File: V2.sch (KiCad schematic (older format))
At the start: 97 parts, among them J1 Extr Cooler 2, J10 MS2, J11 MS3, J12 MS1, J13 MS2, J14 MS3, J15 Extr1 Temp, J16 Extr2 Temp, J17 MS1, J18 MS2, J19 MS3, J2 Extr Cooler 1, J20 Boot0, J21 Bed Temp, J22 Boot1, J23 MS1, J24 MS2, J25 MS3, J26 USB_A, J27 LCD, J28 MS1, J29 MS2, J3 Bed Heater, J30 MS3, J31 USB_A, J4 Extr1 Heater, J5 Extr2 Heater, J6 MS1, J7 MS2, J8 MS3, J9 MS1, M1 Motor E2, M2 Motor E1, M3 Motor Z2, M4 Motor Z1, M5 Motor Y, M6 Motor X, Q1 STN4NF20L, Q2 STN4NF20L, Q3 04N03LA, Q4 04N03LA, Q5 04N03LA, SW1 Bed level, SW10 Button DOWN, SW11 Button UP, SW2 Boundary X, SW3 Boundary Y, SW4 Boundary Z1, SW5 Boundary Z2, SW6 Boundary E1, SW7 Boundary E2, SW8 Button BACK, SW9 Button OK, U1 LM2596S-5, U2 R-783.3-1.0, U3 STM32F105VCT6, U4 CP2104, Y1 8MHz

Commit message: this is layout
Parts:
- removed J31: USB_A, symbol Connector:USB_A
- removed SW1: Bed level, symbol Switch:SW_Push_Open
- added J?: USB_B, symbol Connector:USB_B
- added J?: Bed level, symbol Connector:Conn_01x03_Male
- added LS?: Beeper, symbol device:Speaker
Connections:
- wire segments 497 -> 498
- no-connect marks 39 -> 38
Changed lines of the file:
@@
 Connection ~ 19300 7300
 $Comp
-L Switch:SW_Push_Open SW1
-U 1 1 5C488341
-P 8150 15550
-F 0 "SW1" V 8104 15627 50  0000 L CNN
-F 1 "Bed level" V 8195 15627 50  0000 L CNN
-F 2 "" H 8150 15750 50  0001 C CNN
-F 3 "" H 8150 15750 50  0001 C CNN
-	1    8150 15550
-	0    1    1    0
-$EndComp
-$Comp
 L Switch:SW_Push_Open SW2
 U 1 1 5C491094
@@
 L power:GNDD #PWR0130
 U 1 1 5C497D89
-P 8150 15750
-F 0 "#PWR0130" H 8150 15500 50  0001 C CNN
-F 1 "GNDD" H 8154 15595 50  0000 C CNN
-F 2 "" H 8150 15750 50  0001 C CNN
-F 3 "" H 8150 15750 50  0001 C CNN
-	1    8150 15750
-	1    0    0    -1
+P 8050 15550
+F 0 "#PWR0130" H 8050 15300 50  0001 C CNN
+F 1 "GNDD" H 8054 15395 50  0000 C CNN
+F 2 "" H 8050 15550 50  0001 C CNN
+F 3 "" H 8050 15550 50  0001 C CNN
+	1    8050 15550
+	-1   0    0    1
 $EndComp
 $Comp
@@
 $EndComp
 Wire Wire Line
-	8150 15350 8150 14200
-Wire Wire Line
 	8700 15350 8700 14250
 Wire Wire Line
@@
 L power:GNDD #PWR0137
 U 1 1 5C4C285A
-P 13050 15750
-F 0 "#PWR0137" H 13050 15500 50  0001 C CNN
-F 1 "GNDD" H 13054 15595 50  0000 C CNN
-F 2 "" H 13050 15750 50  0001 C CNN
-F 3 "" H 13050 15750 50  0001 C CNN
-	1    13050 15750
+P 12950 15250
+F 0 "#PWR0137" H 12950 15000 50  0001 C CNN
+F 1 "GNDD" H 12954 15095 50  0000 C CNN
+F 2 "" H 12950 15250 50  0001 C CNN
+F 3 "" H 12950 15250 50  0001 C CNN
+	1    12950 15250
 	1    0    0    -1
 $EndComp
@@
 L power:GNDD #PWR0138
 U 1 1 5C4C289F
-P 14250 15750
-F 0 "#PWR0138" H 14250 15500 50  0001 C CNN
-F 1 "GNDD" H 14254 15595 50  0000 C CNN
-F 2 "" H 14250 15750 50  0001 C CNN
-F 3 "" H 14250 15750 50  0001 C CNN
-	1    14250 15750
+P 14150 15250
+F 0 "#PWR0138" H 14150 15000 50  0001 C CNN
+F 1 "GNDD" H 14154 15095 50  0000 C CNN
+F 2 "" H 14150 15250 50  0001 C CNN
+F 3 "" H 14150 15250 50  0001 C CNN
+	1    14150 15250
 	1    0    0    -1
 $EndComp
@@
 L power:+3.3V #PWR0139
 U 1 1 5C4DF4BB
-P 14150 15250
-F 0 "#PWR0139" H 14150 15100 50  0001 C CNN
-F 1 "+3.3V" H 14165 15423 50  0000 C CNN
-F 2 "" H 14150 15250 50  0001 C CNN
-F 3 "" H 14150 15250 50  0001 C CNN
-	1    14150 15250
+P 14250 15750
+F 0 "#PWR0139" H 14250 15600 50  0001 C CNN
+F 1 "+3.3V" H 14265 15923 50  0000 C CNN
+F 2 "" H 14250 15750 50  0001 C CNN
+F 3 "" H 14250 15750 50  0001 C CNN
+	1    14250 15750
 	-1   0    0    1
 $EndComp
@@
 L power:+3.3V #PWR0140
 U 1 1 5C4DF849
-P 12950 15250
-F 0 "#PWR0140" H 12950 15100 50  0001 C CNN
-F 1 "+3.3V" H 12965 15423 50  0000 C CNN
-F 2 "" H 12950 15250 50  0001 C CNN
-F 3 "" H 12950 15250 50  0001 C CNN
-	1    12950 15250
+P 13050 15750
+F 0 "#PWR0140" H 13050 15600 50  0001 C CNN
+F 1 "+3.3V" H 13065 15923 50  0000 C CNN
+F 2 "" H 13050 15750 50  0001 C CNN
+F 3 "" H 13050 15750 50  0001 C CNN
+	1    13050 15750
 	-1   0    0    1
 $EndComp
@@
 NoConn ~ 8400 10300
 NoConn ~ 8400 10400
-NoConn ~ 8400 12100
 NoConn ~ 13400 12100
 NoConn ~ 13400 10900
@@
 L power:GNDD #PWR0230
 U 1 1 5CC07B42
-P 15500 15750
-F 0 "#PWR0230" H 15500 15500 50  0001 C CNN
-F 1 "GNDD" H 15504 15595 50  0000 C CNN
-F 2 "" H 15500 15750 50  0001 C CNN
-F 3 "" H 15500 15750 50  0001 C CNN
-	1    15500 15750
+P 15400 15250
+F 0 "#PWR0230" H 15400 15000 50  0001 C CNN
+F 1 "GNDD" H 15404 15095 50  0000 C CNN
+F 2 "" H 15400 15250 50  0001 C CNN
+F 3 "" H 15400 15250 50  0001 C CNN
+	1    15400 15250
 	1    0    0    -1
 $EndComp
@@
 L power:+3.3V #PWR0231
 U 1 1 5CC07B4A
-P 15400 15250
-F 0 "#PWR0231" H 15400 15100 50  0001 C CNN
-F 1 "+3.3V" H 15415 15423 50  0000 C CNN
-F 2 "" H 15400 15250 50  0001 C CNN
-F 3 "" H 15400 15250 50  0001 C CNN
-	1    15400 15250
+P 15500 15750
+F 0 "#PWR0231" H 15500 15600 50  0001 C CNN
+F 1 "+3.3V" H 15515 15923 50  0000 C CNN
+F 2 "" H 15500 15750 50  0001 C CNN
+F 3 "" H 15500 15750 50  0001 C CNN
+	1    15500 15750
 	-1   0    0    1
 $EndComp
@@
 Wire Wire Line
 	14950 6800 14950 8200
-$Comp
-L Connector:USB_A J31
-U 1 1 5D21B69F
-P 22150 12950
-F 0 "J31" H 22205 13417 50  0000 C CNN
-F 1 "USB_A" H 22205 13326 50  0000 C CNN
-F 2 "" H 22300 12900 50  0001 C CNN
-F 3 "" H 22300 12900 50  0001 C CNN
-	1    22150 12950
-	-1   0    0    1
-$EndComp
 Wire Wire Line
 	13400 9500 16500 9500
@@
 NoConn ~ 13400 9900
 NoConn ~ 13400 10000
+$Comp
+L Connector:USB_B J?
+U 1 1 5C4EAA49
+P 22150 12950
+F 0 "J?" H 22150 13400 50  0000 R CNN
+F 1 "USB_B" H 22250 13300 50  0000 R CNN
+F 2 "" H 22300 12900 50  0001 C CNN
+F 3 "" H 22300 12900 50  0001 C CNN
+	1    22150 12950
+	-1   0    0    1
+$EndComp
+$Comp
+L device:Speaker LS?
+U 1 1 5C58EC92
+P 8600 12700
+F 0 "LS?" H 8770 12696 50  0000 L CNN
+F 1 "Beeper" H 8770 12605 50  0000 L CNN
+F 2 "" H 8600 12500 50  0001 C CNN
+F 3 "" H 8590 12650 50  0001 C CNN
+	1    8600 12700
+	1    0    0    -1
+$EndComp
+Wire Wire Line
+	8400 12700 8400 12100
+$Comp
+L power:GNDD #PWR?
+U 1 1 5C61EBE1
+P 8400 12800
+F 0 "#PWR?" H 8400 12550 50  0001 C CNN
+F 1 "GNDD" V 8500 12800 50  0000 R CNN
+F 2 "" H 8400 12800 50  0001 C CNN
+F 3 "" H 8400 12800 50  0001 C CNN
+	1    8400 12800
+	0    1    1    0
+$EndComp
+$Comp
+L Connector:Conn_01x03_Male J?
+U 1 1 5C6206CB
+P 8150 15750
+F 0 "J?" V 8000 15750 50  0000 R CNN
+F 1 "Bed level" V 8100 15900 50  0000 R CNN
+F 2 "" H 8150 15750 50  0001 C CNN
+F 3 "~" H 8150 15750 50  0001 C CNN
+	1    8150 15750
+	0    -1   -1   0
+$EndComp
+$Comp
+L power:+3.3V #PWR?
+U 1 1 5C789638
+P 8250 15550
+F 0 "#PWR?" H 8250 15400 50  0001 C CNN
+F 1 "+3.3V" H 8265 15723 50  0000 C CNN
+F 2 "" H 8250 15550 50  0001 C CNN
+F 3 "" H 8250 15550 50  0001 C CNN
+	1    8250 15550
+	1    0    0    -1
+$EndComp
+Wire Wire Line
+	8150 14200 8150 15550
 $EndSCHEMATC

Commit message: Fix ERC
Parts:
- 33uH1: symbol device:L -> V2-rescue:L-device
- A1, A2, A3, A4, A5, A6: symbol modules:Pololu_Breakout_A4988 -> V2-rescue:Pololu_Breakout_A4988-modules
- C1, C2, C7, C9: symbol device:CP -> V2-rescue:CP-device
- C10, C11, C12, C13, C14, C15, C16, C17, C18, C3, C4, C5, C6, C8: symbol device:C -> V2-rescue:C-device
- D1: symbol Diode:1N5820 -> V2-rescue:1N5820-Diode
- D2: symbol device:D_Schottky -> V2-rescue:D_Schottky-device
- D3, D4: symbol device:LED -> V2-rescue:LED-device
- J1, J15, J16, J2, J20, J21, J22, J3, J4, J5: symbol Connector:Conn_01x02_Male -> V2-rescue:Conn_01x02_Male-Connector
- J10, J11, J12, J13, J14, J17, J18, J19, J23, J24, J25, J28, J29, J30, J6, J7, J8, J9: symbol Connector:Conn_01x03_Male -> V2-rescue:Conn_01x03_Male-Connector
- J26: symbol Connector:USB_A -> V2-rescue:USB_A-Connector
- J27: symbol Connector:Conn_01x16_Male -> V2-rescue:Conn_01x16_Male-Connector
- J31: renamed from J?; symbol Connector:Conn_01x03_Male -> V2-rescue:Conn_01x03_Male-Connector
- J32: renamed from J?; symbol Connector:USB_B -> V2-rescue:USB_B-Connector
- LS1: renamed from LS?; symbol device:Speaker -> V2-rescue:Speaker-device
- M1, M2, M3, M4, M5, M6: symbol Motor:Stepper_Motor_bipolar -> V2-rescue:Stepper_Motor_bipolar-Motor
- Q1, Q2: symbol Transistor:BSP129 -> V2-rescue:BSP129-Transistor
- Q3, Q4, Q5: symbol Transistor:BSS138 -> V2-rescue:BSS138-Transistor
- R1, R10, R2, R3, R4, R5, R6, R7, R8, R9: symbol device:R -> V2-rescue:R-device
- SW10, SW11, SW8, SW9: symbol Switch:SW_Push -> V2-rescue:SW_Push-Switch
- SW2, SW3, SW4, SW5, SW6, SW7: symbol Switch:SW_Push_Open -> V2-rescue:SW_Push_Open-Switch
- U1: symbol dc-dc:LM2596S-5 -> V2-rescue:LM2596S-5-dc-dc
- U2: symbol dc-dc:R-783.3-1.0 -> V2-rescue:R-783.3-1.0-dc-dc
- U3: symbol MCU_ST_STM32:STM32F105VCTx -> V2-rescue:STM32F105VCTx-MCU_ST_STM32
- U4: symbol silabs:CP2104 -> V2-rescue:CP2104-silabs
- Y1: symbol device:Crystal -> V2-rescue:Crystal-device
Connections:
- net labels added: VBUS
- wire segments 498 -> 503

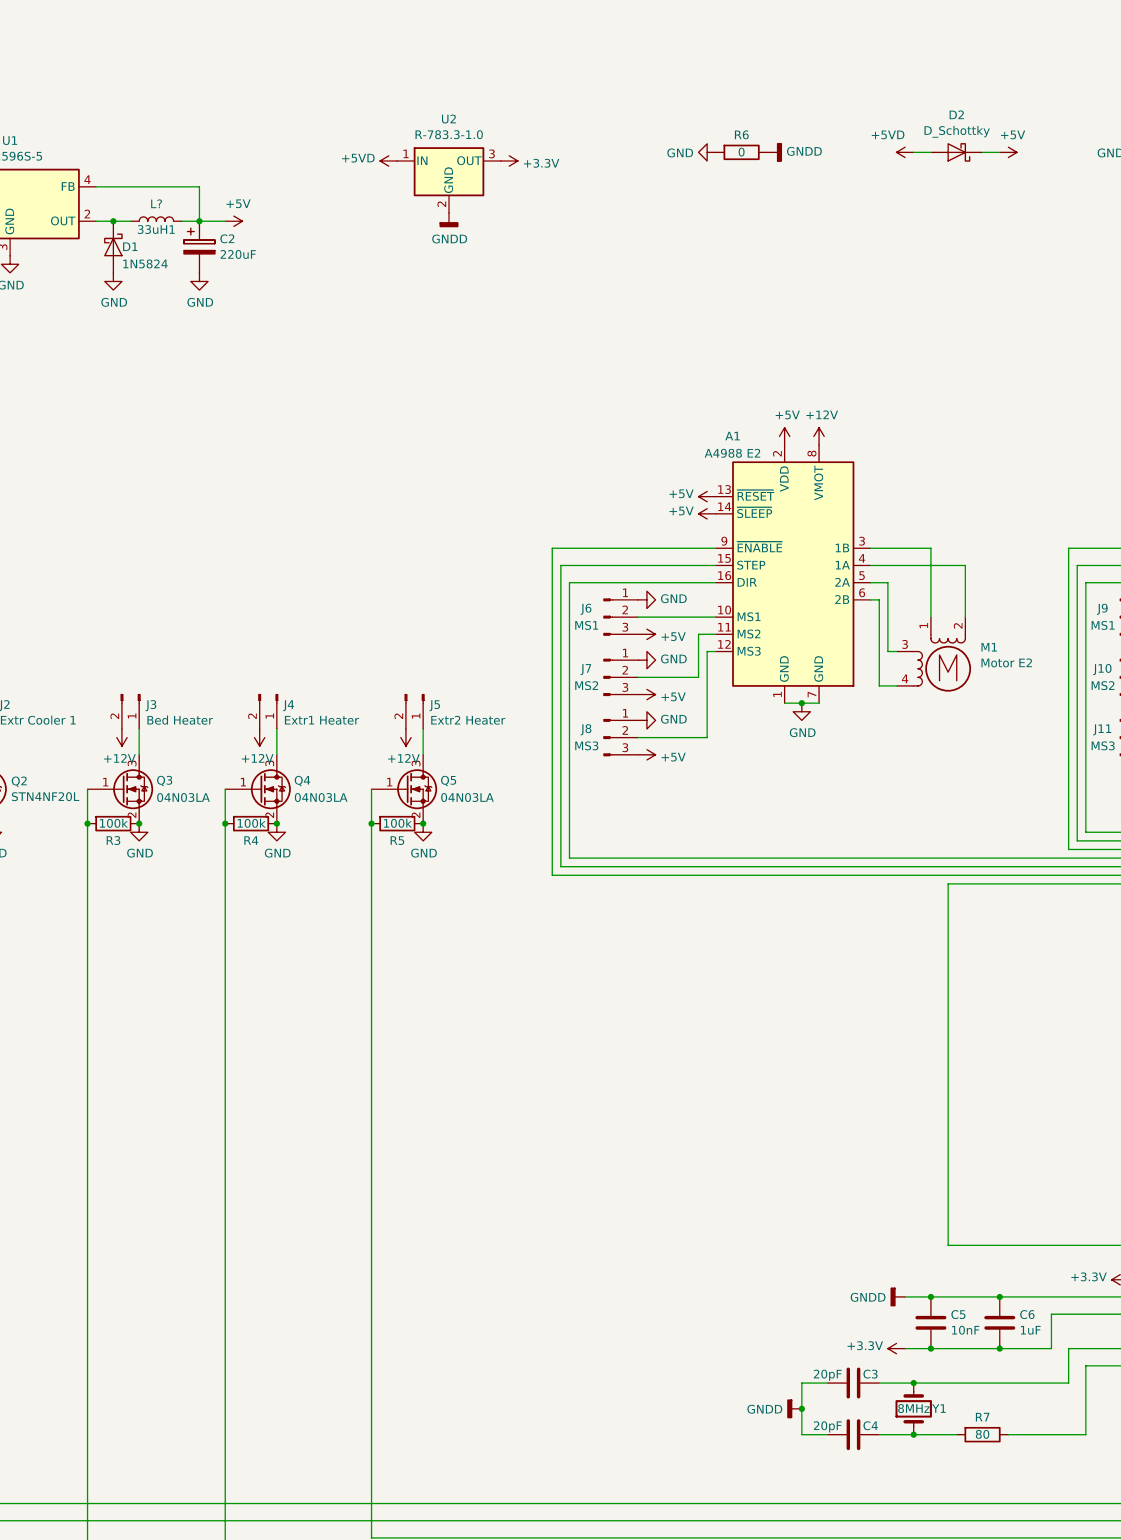
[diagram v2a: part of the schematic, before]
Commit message: footprints are added
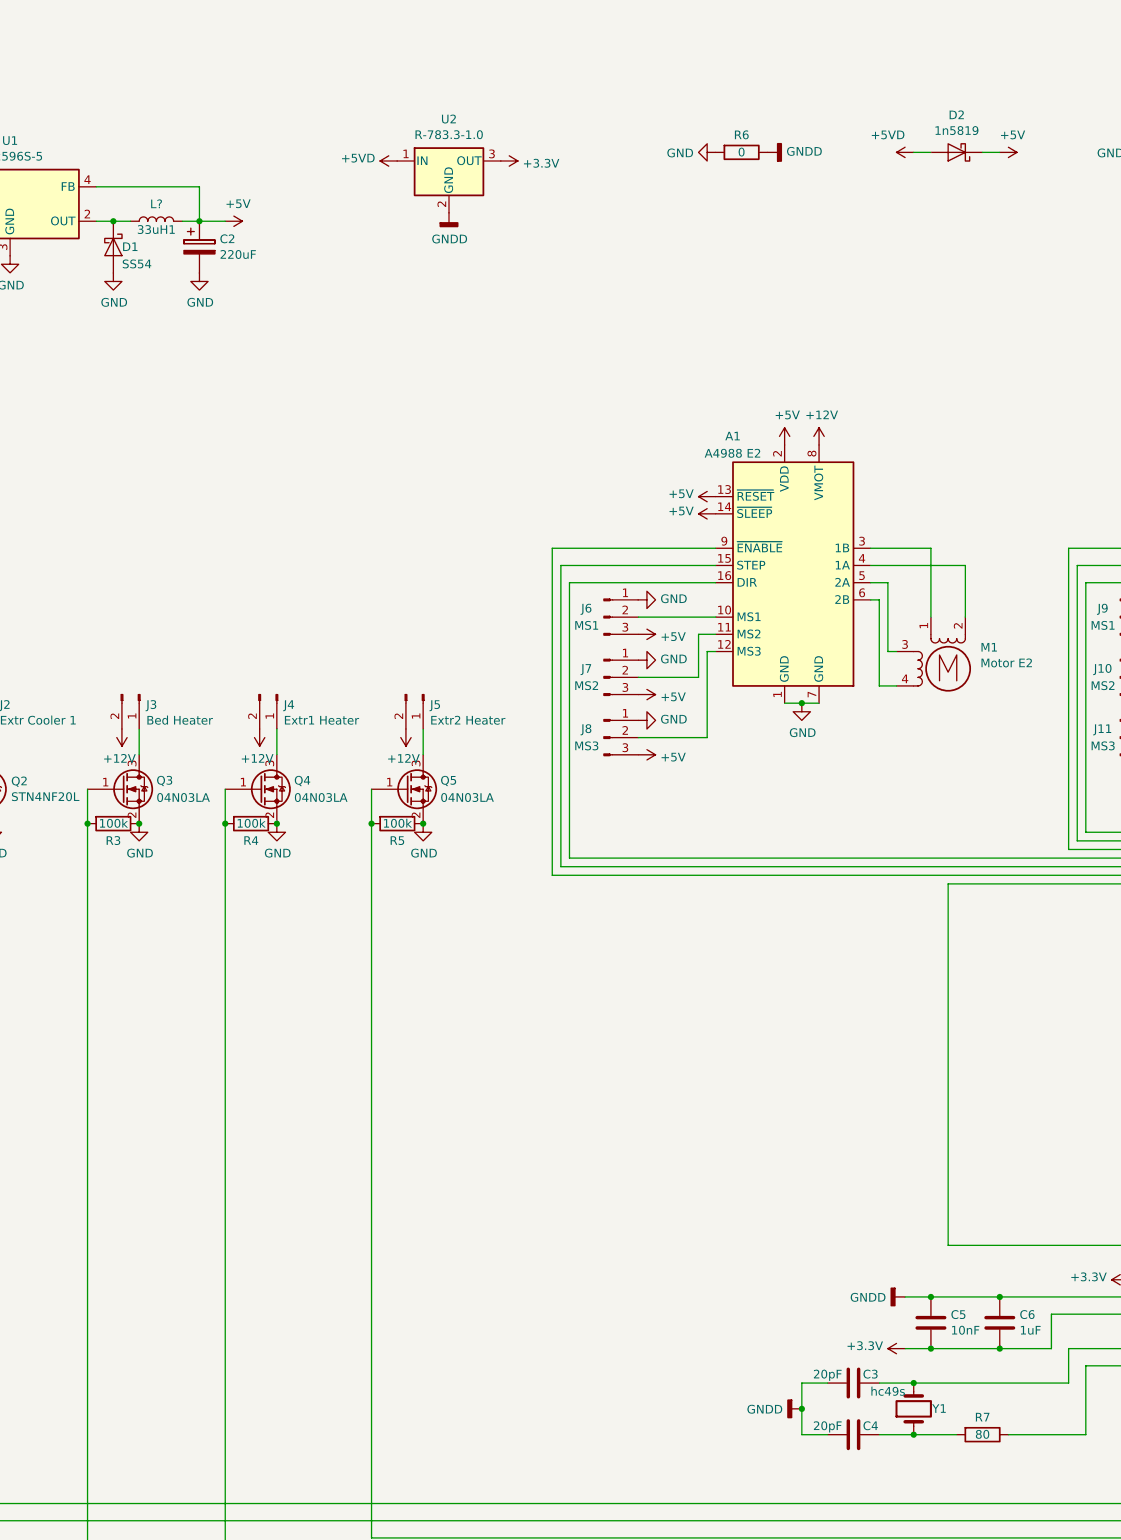
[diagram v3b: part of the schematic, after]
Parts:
- 33uH1: footprint (none) -> Inductor_SMD:L_1206_3216Metric
- A1, A2, A3, A4, A5, A6: footprint Modules:Pololu_Breakout-16_15.2x20.3mm -> Module:Pololu_Breakout-16_15.2x20.3mm
- C1, C2: footprint (none) -> Capacitor_SMD:CP_Elec_10x10.5
- C10, C11, C12, C13, C14, C15, C16, C17, C18, C3, C4, C5, C6, C8: footprint (none) -> Capacitor_SMD:C_1206_3216Metric
- C7, C9: footprint (none) -> Capacitor_SMD:CP_Elec_6.3x5.4
- D1: value 1N5824 -> SS54; footprint Diodes_THT:D_DO-201AD_Horizontal_RM15 -> Diode_SMD:D_2512_6332Metric_Castellated
- D2: value D_Schottky -> 1n5819; footprint (none) -> w_smd_diode:do214ac
- D3, D4: footprint (none) -> w_smd_leds:Led_0402
- J1, J15, J16, J2, J20, J21, J22, J3, J31, J4, J5, LS1, SW10, SW11, SW2, SW3, SW4, SW5, SW6, SW7, SW8, SW9: footprint (none) -> Connector_PinHeader_2.54mm:PinHeader_1x02_P2.54mm_Vertical_SMD_Pin1Left
- J10, J11, J12, J13, J14, J17, J18, J19, J23, J24, J25, J28, J29, J30, J6, J7, J8, J9: footprint (none) -> Connector_PinHeader_2.54mm:PinHeader_1x03_P2.54mm_Vertical_SMD_Pin1Left
- J26: footprint (none) -> Connector_USB:USB_A_CNCTech_1001-011-01101_Horizontal
- J27: footprint (none) -> w_indicators:lcd_20x4
- J32: footprint (none) -> Connector_USB:USB_B_Amphenol_MUSB-D511_Vertical_Rugged
- M1, M2, M3, M4, M5, M6: footprint (none) -> Connector_PinHeader_2.54mm:PinHeader_1x04_P2.54mm_Vertical_SMD_Pin1Left
- Q1, Q2: footprint TO_SOT_Packages_SMD:SOT-223-3_TabPin2 -> Package_TO_SOT_SMD:SOT-223-3_TabPin2
- Q3, Q4, Q5: footprint TO_SOT_Packages_SMD:TO-252 -> Package_TO_SOT_SMD:TO-252-3_TabPin2
- R1, R10, R2, R3, R4, R5, R7, R8, R9: footprint (none) -> Resistor_SMD:R_1206_3216Metric
- R6: footprint (none) -> Resistor_SMD:R_0201_0603Metric
- U1: footprint TO_SOT_Packages_SMD:TO-263-5_TabPin3 -> Package_TO_SOT_SMD:TO-263-5_TabPin3
- U2: footprint Converters_DCDC_ACDC:DCDC-Conv_RECOM_R-78E-0.5 -> Package_TO_SOT_SMD:TO-252-3_TabPin2
- U3: footprint LQFP100 -> Package_QFP:LQFP-100_14x14mm_P0.5mm
- U4: footprint Housings_DFN_QFN:QFN-24-1EP_4x4mm_Pitch0.5mm -> Package_DFN_QFN:QFN-24-1EP_4x4mm_P0.5mm_EP2.7x2.7mm
- Y1: value 8MHz -> hc49s; footprint (none) -> Crystal:Crystal_SMD_HC49-SD

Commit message: много изменений, поэтому новый бранч
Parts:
- removed J1: Extr Cooler 2, Connector_PinHeader_2.54mm:PinHeader_1x02_P2.54mm_Vertical_SMD_Pin1Left, symbol V2-rescue:Conn_01x02_Male-Connector
- removed J10, J13, J18, J24, J29, J7: MS2, Connector_PinHeader_2.54mm:PinHeader_1x03_P2.54mm_Vertical_SMD_Pin1Left, symbol V2-rescue:Conn_01x03_Male-Connector
- removed J11, J14, J19, J25, J30, J8: MS3, Connector_PinHeader_2.54mm:PinHeader_1x03_P2.54mm_Vertical_SMD_Pin1Left, symbol V2-rescue:Conn_01x03_Male-Connector
- removed J12, J17, J23, J28, J6, J9: MS1, Connector_PinHeader_2.54mm:PinHeader_1x03_P2.54mm_Vertical_SMD_Pin1Left, symbol V2-rescue:Conn_01x03_Male-Connector
- removed J15: Extr1 Temp, Connector_PinHeader_2.54mm:PinHeader_1x02_P2.54mm_Vertical_SMD_Pin1Left, symbol V2-rescue:Conn_01x02_Male-Connector
- removed J16: Extr2 Temp, Connector_PinHeader_2.54mm:PinHeader_1x02_P2.54mm_Vertical_SMD_Pin1Left, symbol V2-rescue:Conn_01x02_Male-Connector
- removed J2: Extr Cooler 1, Connector_PinHeader_2.54mm:PinHeader_1x02_P2.54mm_Vertical_SMD_Pin1Left, symbol V2-rescue:Conn_01x02_Male-Connector
- removed J4: Extr1 Heater, Connector_PinHeader_2.54mm:PinHeader_1x02_P2.54mm_Vertical_SMD_Pin1Left, symbol V2-rescue:Conn_01x02_Male-Connector
- removed J5: Extr2 Heater, Connector_PinHeader_2.54mm:PinHeader_1x02_P2.54mm_Vertical_SMD_Pin1Left, symbol V2-rescue:Conn_01x02_Male-Connector
- removed M1: Motor E2, Connector_PinHeader_2.54mm:PinHeader_1x04_P2.54mm_Vertical_SMD_Pin1Left, symbol V2-rescue:Stepper_Motor_bipolar-Motor
- removed M2: Motor E1, Connector_PinHeader_2.54mm:PinHeader_1x04_P2.54mm_Vertical_SMD_Pin1Left, symbol V2-rescue:Stepper_Motor_bipolar-Motor
- added J6: Head2, Connector_JST:JST_EH_B09B-EH-A_1x09_P2.50mm_Vertical, symbol Connector:Conn_01x09
- added J7: Head1, Connector_JST:JST_EH_B09B-EH-A_1x09_P2.50mm_Vertical, symbol Connector:Conn_01x09
- added Q6: 04N03LA, Package_TO_SOT_SMD:TO-252-3_TabPin2, symbol V2-rescue:BSS138-Transistor
- added R11: 100k, Resistor_SMD:R_1206_3216Metric, symbol V2-rescue:R-device
- D3, D4: footprint w_smd_leds:Led_0402 -> LED_THT:LED_D1.8mm_W1.8mm_H2.4mm_Horizontal_O1.27mm_Z1.6mm
- J20, J22, SW10, SW11, SW8, SW9: footprint Connector_PinHeader_2.54mm:PinHeader_1x02_P2.54mm_Vertical_SMD_Pin1Left -> Connector_PinHeader_2.54mm:PinHeader_1x02_P2.54mm_Vertical
- J21, SW2, SW3, SW4, SW5, SW6, SW7: footprint Connector_PinHeader_2.54mm:PinHeader_1x02_P2.54mm_Vertical_SMD_Pin1Left -> Connector_JST:JST_EH_B02B-EH-A_1x02_P2.50mm_Vertical
- J26: footprint Connector_USB:USB_A_CNCTech_1001-011-01101_Horizontal -> w_conn_pc:conn_usb_A-vert2
- J3: footprint Connector_PinHeader_2.54mm:PinHeader_1x02_P2.54mm_Vertical_SMD_Pin1Left -> TerminalBlock_4Ucon:TerminalBlock_4Ucon_1x02_P3.50mm_Horizontal
- J31: footprint Connector_PinHeader_2.54mm:PinHeader_1x02_P2.54mm_Vertical_SMD_Pin1Left -> Connector_PinHeader_2.54mm:PinHeader_1x03_P2.54mm_Vertical_SMD_Pin1Left
- LS1: footprint Connector_PinHeader_2.54mm:PinHeader_1x02_P2.54mm_Vertical_SMD_Pin1Left -> Buzzer_Beeper:Buzzer_12x9.5RM7.6
- M3, M4, M5, M6: footprint Connector_PinHeader_2.54mm:PinHeader_1x04_P2.54mm_Vertical_SMD_Pin1Left -> Connector_JST:JST_EH_S04B-EH_1x04_P2.50mm_Horizontal
- R6: footprint Resistor_SMD:R_0201_0603Metric -> Resistor_SMD:R_0603_1608Metric
- Y1: footprint Crystal:Crystal_SMD_HC49-SD -> Crystal:Crystal_HC49-4H_Vertical
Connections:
- net labels added: +24V
- net labels removed: +12V
- wire segments 503 -> 516
- no-connect marks 38 -> 37
